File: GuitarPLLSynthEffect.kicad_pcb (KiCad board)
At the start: 2 copper layers, 83.1 x 165.1 mm, 67 parts

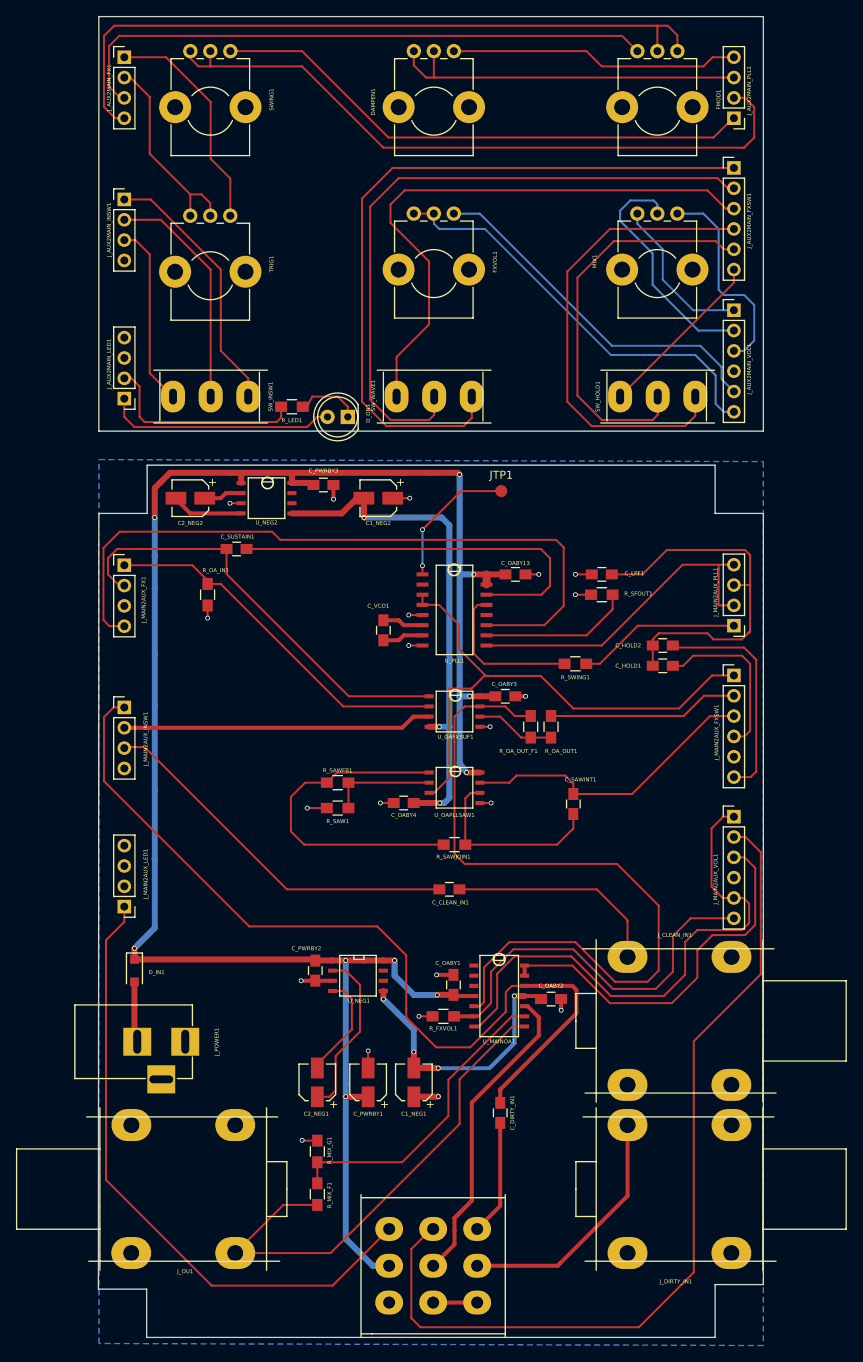
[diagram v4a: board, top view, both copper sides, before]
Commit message: Board Redesign - RevB
- Created seperate ground plane for DC-DC Converters
- Re-routed the rest of the board.
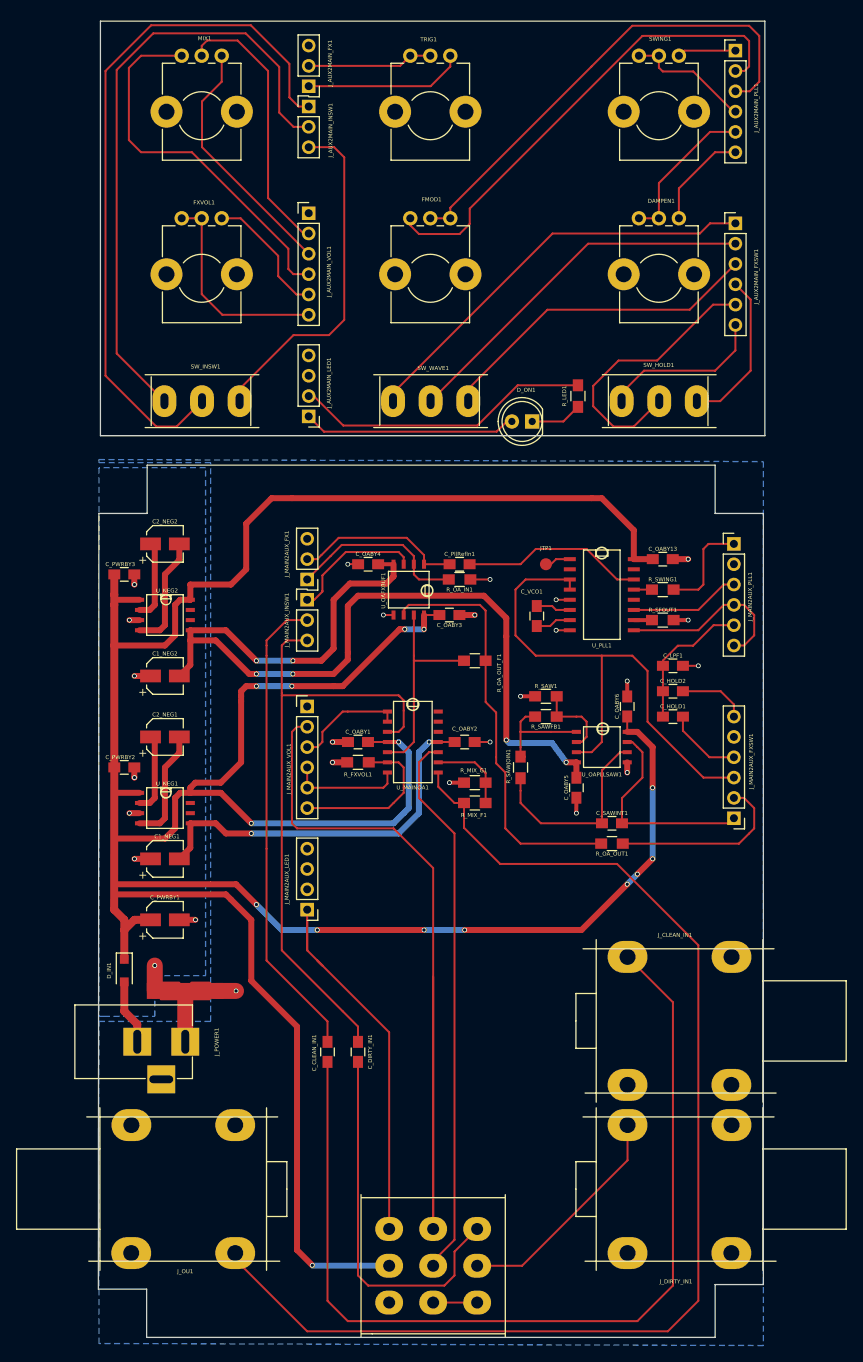
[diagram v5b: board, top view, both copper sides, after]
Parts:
- removed C_SUSTAIN1: 47nF, Capacitors_SMD:C_0805_HandSoldering
- added C_OABY5: 100nF, Capacitors_SMD:C_0805_HandSoldering, F.Cu at (117.5, 148.6)
- added C_OABY6: 100nF, Capacitors_SMD:C_0805_HandSoldering, F.Cu at (123.8, 138.4)
- added C_PllRefIn1: 47nF, Capacitors_SMD:C_0805_HandSoldering, F.Cu at (102.9, 120.7)
- added JP_MIXEDGND1: Jumper_NC_Dual, Oddities:NetTie-II_Connected_SMD, F.Cu at (68.6, 174.0)
- J_AUX2MAIN_FX1, J_AUX2MAIN_INSW1, J_MAIN2AUX_FX1, J_MAIN2AUX_INSW1: value Conn_01x04 -> Conn_01x03; footprint Pin_Headers:Pin_Header_Straight_1x04_Pitch2.54mm -> Pin_Headers:Pin_Header_Straight_1x03_Pitch2.54mm
- J_AUX2MAIN_PLL1, J_MAIN2AUX_PLL1: value Conn_01x04 -> Conn_01x06; footprint Pin_Headers:Pin_Header_Straight_1x04_Pitch2.54mm -> Pin_Headers:Pin_Header_Straight_1x06_Pitch2.54mm
- moved MIX1 60.3 mm to (68.1, 57.1)
- moved SWING1 56.1 mm to (125.3, 57.1)
- moved J_MAIN2AUX_VOL1 55.1 mm to (83.8, 138.4)
- moved J_AUX2MAIN_VOL1 54.5 mm to (84.0, 76.8)
- moved R_MIX_F1 52.7 mm to (104.8, 150.5), turned to 0 degrees
- moved R_MIX_G1 50.1 mm to (104.8, 148.0), turned to 0 degrees
- moved C2_NEG1 47.2 mm to (66.0, 142.2), turned to 0 degrees
- moved C1_NEG1 41.8 mm to (66.0, 157.5), turned to 0 degrees
- moved R_LED1 35.8 mm to (117.7, 99.6), turned to 90 degrees
- moved FMOD1 35.2 mm to (96.7, 77.4)
- moved DAMPEN1 35.0 mm to (125.3, 77.4)
- moved C_PWRBY2 34.9 mm to (61.0, 146.1), turned to 180 degrees
- moved C1_NEG2 34.7 mm to (66.0, 134.6), turned to 0 degrees
- moved TRIG1 34.0 mm to (96.7, 57.1)
- moved C_OABY2 33.9 mm to (103.5, 142.9)
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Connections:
- C1_NEG1 pad 1: /GND -> /DGND
- C1_NEG2 pad 1: /GND -> /DGND
- C_PWRBY1 pad 2: /GND -> /DGND
- C_PWRBY2 pad 1: /GND -> /DGND
- C_PWRBY3 pad 1: /GND -> /DGND
- J_AUX2MAIN_FX1 pad 3: Net-(FMOD1-Pad1) -> Net-(J_AUX2MAIN_FX1-Pad3)
- J_AUX2MAIN_LED1 pad 3: (no net) -> Net-(J_AUX2MAIN_LED1-Pad3)
- J_AUX2MAIN_LED1 pad 4: (no net) -> Net-(J_AUX2MAIN_LED1-Pad4)
- J_AUX2MAIN_PLL1 pad 2: Net-(J_AUX2MAIN_PLL1-Pad2) -> Net-(FMOD1-Pad1)
- J_AUX2MAIN_PLL1 pad 3: Net-(DAMPEN1-Pad1) -> Net-(FMOD1-Pad2)
- J_AUX2MAIN_PLL1 pad 4: Net-(DAMPEN1-Pad3) -> Net-(J_AUX2MAIN_PLL1-Pad4)
- J_AUX2MAIN_VOL1 pad 4: (no net) -> Net-(J_AUX2MAIN_VOL1-Pad4)
- J_CLEAN_IN1 pad 3: (no net) -> Net-(J_CLEAN_IN1-Pad3)
- J_DIRTY_IN1 pad 3: (no net) -> Net-(J_DIRTY_IN1-Pad3)
- J_MAIN2AUX_FX1 pad 3: /GND -> Net-(J_MAIN2AUX_FX1-Pad3)
- J_MAIN2AUX_FXSW1 pad 1: /Sheet5AC1BF71/VCORETURN -> /Sheet5AC1BF71/WAVESEL_P3
- J_MAIN2AUX_FXSW1 pad 3: /Sheet5AC1BF71/WAVESEL_P3 -> /Sheet5AC1BF71/VCORETURN
- J_MAIN2AUX_INSW1 pad 1: /INSW_P1 -> /INSW_P2
- J_MAIN2AUX_INSW1 pad 2: /INSW_P2 -> /INSW_P3
- J_MAIN2AUX_INSW1 pad 3: /INSW_P3 -> /INSW_P1
- J_MAIN2AUX_LED1 pad 3: (no net) -> Net-(J_MAIN2AUX_LED1-Pad3)
- J_MAIN2AUX_LED1 pad 4: (no net) -> Net-(J_MAIN2AUX_LED1-Pad4)
- J_MAIN2AUX_PLL1 pad 2: /Sheet5AC1BF71/DAMP_P3 -> /GND
- J_MAIN2AUX_PLL1 pad 3: /Sheet5AC1BF71/DAMP_P1_2 -> /Sheet5AC1BF71/FMOD_P2_P3
- J_MAIN2AUX_VOL1 pad 1: /FXVOL_P3 -> Net-(J_MAIN2AUX_VOL1-Pad1)
- J_MAIN2AUX_VOL1 pad 4: (no net) -> /FXVOL_P3
- J_OU1 pad 2: (no net) -> Net-(J_OU1-Pad2)
- J_OU1 pad 3: (no net) -> Net-(J_OU1-Pad3)
- J_POWER1 pad 1: /GND -> Net-(JP_MIXEDGND1-Pad2)
- J_POWER1 pad 3: (no net) -> Net-(J_POWER1-Pad3)
- MIX1 pad 1: Net-(J_AUX2MAIN_VOL1-Pad1) -> Net-(J_AUX2MAIN_VOL1-Pad4)
- SWING1 pad 1: Net-(J_AUX2MAIN_PLL1-Pad2) -> Net-(J_AUX2MAIN_PLL1-Pad4)
- SWING1 pad 2: Net-(J_AUX2MAIN_PLL1-Pad2) -> Net-(J_AUX2MAIN_PLL1-Pad4)
- SW_BYPASS1 pad 7: (no net) -> Net-(SW_BYPASS1-Pad7)
- SW_INSW1 pad 1: Net-(J_AUX2MAIN_INSW1-Pad1) -> Net-(J_AUX2MAIN_INSW1-Pad3)
- SW_INSW1 pad 2: Net-(J_AUX2MAIN_INSW1-Pad2) -> Net-(J_AUX2MAIN_INSW1-Pad1)
- SW_INSW1 pad 3: Net-(J_AUX2MAIN_INSW1-Pad3) -> Net-(J_AUX2MAIN_INSW1-Pad2)
- SW_WAVE1 pad 1: Net-(J_AUX2MAIN_FXSW1-Pad1) -> Net-(J_AUX2MAIN_FXSW1-Pad3)
- SW_WAVE1 pad 3: Net-(J_AUX2MAIN_FXSW1-Pad3) -> Net-(J_AUX2MAIN_FXSW1-Pad1)
- U_MAINOA1 pad 1: (no net) -> /MIX_P3
- U_MAINOA1 pad 12: /INSW_P1 -> Net-(U_MAINOA1-Pad12)
- U_MAINOA1 pad 13: /MIX_P3 -> Net-(U_MAINOA1-Pad13)
- U_MAINOA1 pad 14: /MIX_P3 -> Net-(U_MAINOA1-Pad14)
- U_MAINOA1 pad 2: (no net) -> /MIX_P3
- U_MAINOA1 pad 3: (no net) -> /INSW_P1
- U_NEG1 pad 3: /GND -> /DGND
- U_NEG1 pad 6: (no net) -> Net-(U_NEG1-Pad6)
- U_NEG1 pad 7: (no net) -> Net-(U_NEG1-Pad7)
- U_NEG2 pad 3: /GND -> /DGND
- U_NEG2 pad 6: (no net) -> Net-(U_NEG2-Pad6)
- U_NEG2 pad 7: (no net) -> Net-(U_NEG2-Pad7)
- U_PLL1 pad 12: (no net) -> Net-(U_PLL1-Pad12)
- U_PLL1 pad 15: /9V -> Net-(U_PLL1-Pad15)
- U_PLL1 pad 2: (no net) -> Net-(U_PLL1-Pad2)
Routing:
- net /9V: track 245.0 -> 433.4 mm, vias 10 -> 15
- net Net-(C_CLEAN_IN1-Pad1): track 28.1 -> 119.4 mm
- net Net-(J_OU1-Pad1): track 63.9 -> 152.7 mm
- net Net-(J_AUX2MAIN_PLL1-Pad2): track 85.9 -> 0.00 mm
- net /Sheet5AC1BF71/FMOD_P2_P3: track 89.1 -> 13.8 mm
- net /Sheet5AC1BF71/SIG_OUT: track 95.7 -> 26.0 mm
- net Net-(J_AUX2MAIN_PLL1-Pad1): track 68.7 -> 7.33 mm
- net /Sheet5AC1BF71/-9V: track 64.6 -> 122.4 mm, vias 3 -> 6
- net Net-(J_AUX2MAIN_INSW1-Pad1): track 33.0 -> 88.5 mm
- net /FXVOL_P3: track 68.1 -> 14.3 mm
- net Net-(J_AUX2MAIN_INSW1-Pad2): track 29.2 -> 78.0 mm
- net Net-(J_AUX2MAIN_VOL1-Pad4): track 0.00 -> 47.2 mm
- net Net-(R_OA_OUT1-Pad1): track 9.98 -> 53.1 mm
- net Net-(J_AUX2MAIN_FXSW1-Pad4): track 61.7 -> 19.9 mm
- net Net-(J_AUX2MAIN_FXSW1-Pad1): track 91.5 -> 52.6 mm
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- added copper zone on B.Cu, net /DGND
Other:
- board size 83.1 x 165.1 mm -> 83.3 x 164.5 mm
- board text added: "PLL SYNTH RevB Chris Sutton"

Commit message: board correction
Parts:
- moved J_AUX2MAIN_FXSW1 12.8 mm to (137.4, 90.8), turned to 180 degrees
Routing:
- net Net-(J_AUX2MAIN_FXSW1-Pad6): track 20.6 -> 46.7 mm
- net Net-(J_AUX2MAIN_FXSW1-Pad2): track 46.3 -> 67.2 mm
- net Net-(J_AUX2MAIN_FXSW1-Pad3): track 41.4 -> 49.7 mm
- net /LED_ANODE: track 49.1 -> 45.3 mm
- net Net-(J_AUX2MAIN_FXSW1-Pad4): track 19.9 -> 22.8 mm
- net Net-(J_AUX2MAIN_FXSW1-Pad1): track 52.6 -> 50.6 mm
- net Net-(J_AUX2MAIN_FXSW1-Pad5): track 35.2 -> 34.3 mm
